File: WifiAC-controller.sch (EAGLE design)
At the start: 16 parts, among them U1 ATMEGA328P_TQFP

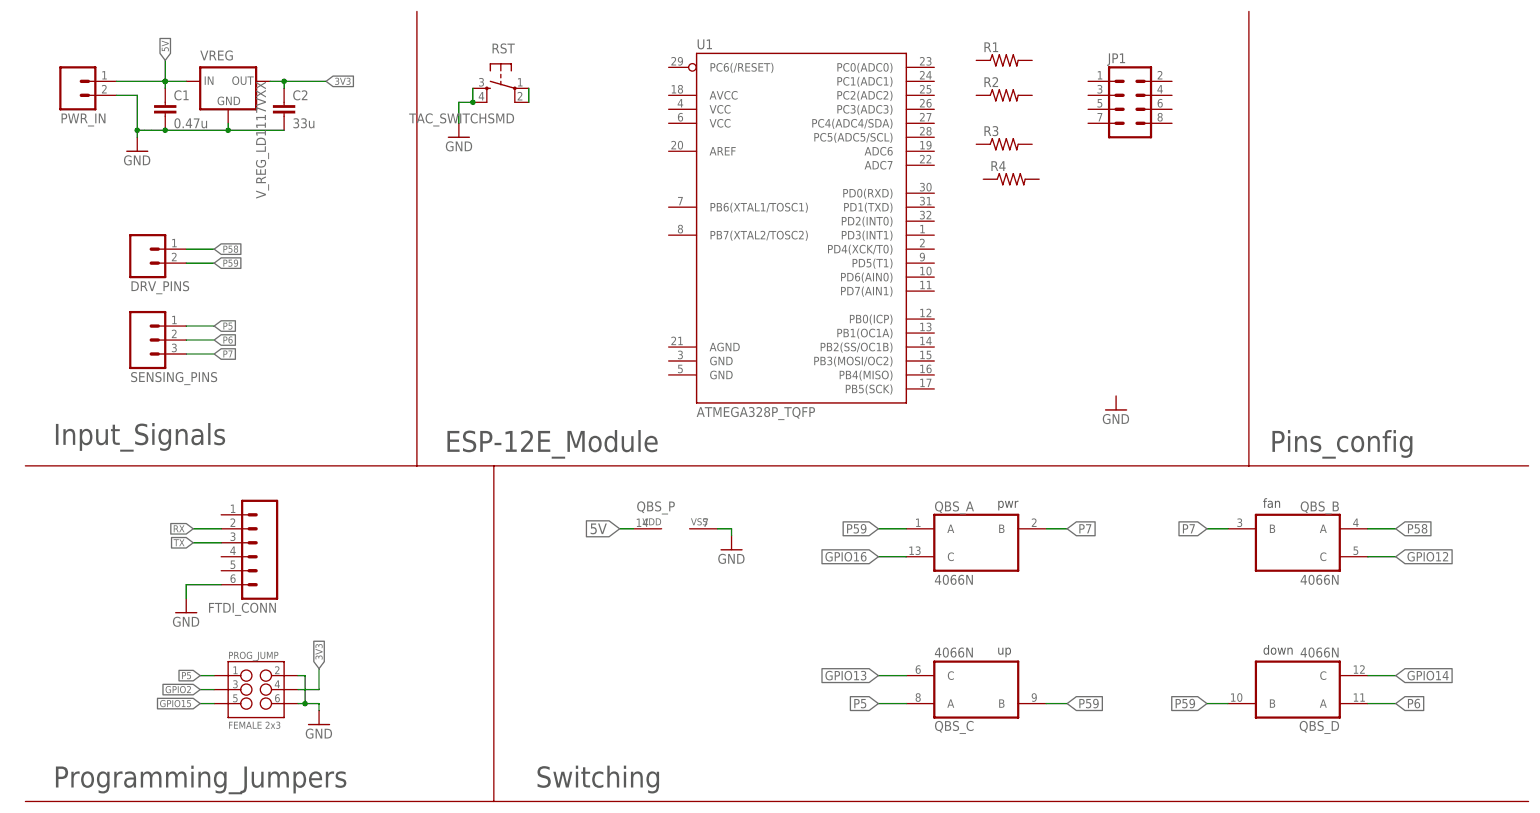
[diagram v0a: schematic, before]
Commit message: updated the circuit and the output file. circuit update includes changing the esp package and adding an atmega328 as mcu
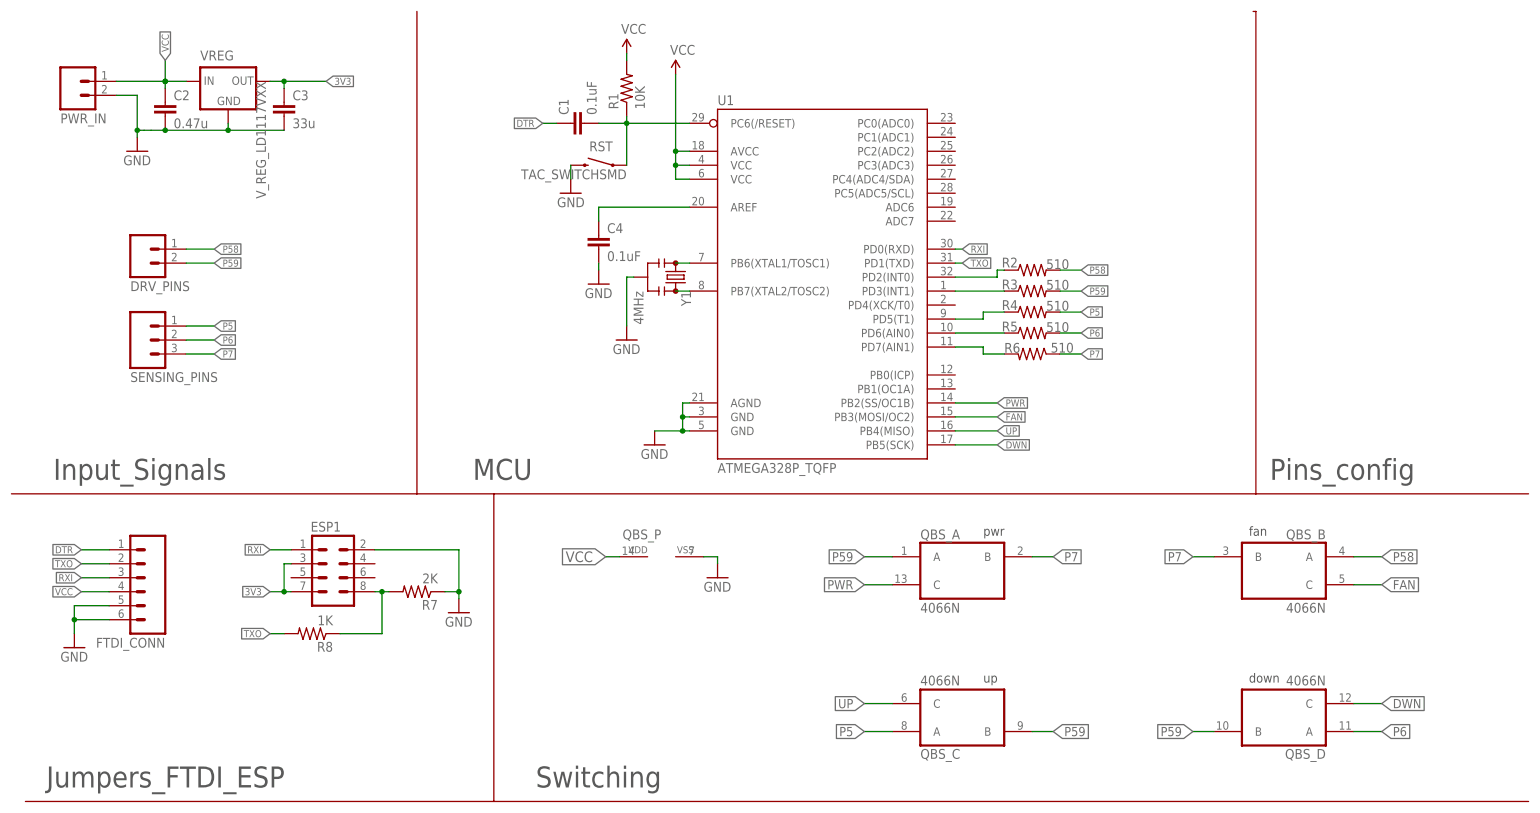
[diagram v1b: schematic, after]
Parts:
- removed JP1: (no value), SparkFun-Connectors:M04X2
- removed PROG_JUMP: FEMALE 2x3, SparkFun-Connectors:M03X2FEMALE
- added C3: 33u, SparkFun-Passives:CAPPTH2
- added C4: 0.1uF, SparkFun-Passives:CAP0805
- added ESP1: (no value), SparkFun-Connectors:M04X2
- added R5, R6: 510, SparkFun-Passives:RESISTOR0805-RES
- added R7: 2K, SparkFun-Passives:RESISTOR0805-RES
- added R8: 1K, SparkFun-Passives:RESISTOR0805-RES
- added Y1: 4MHz, SparkFun-FreqCtrl:RESONATOR4MHZ
- C1: value 0.47u -> 0.1uF; device SparkFun-Passives:CAPEZ -> SparkFun-Passives:CAP0805
- C2: value 33u -> 0.47u; device SparkFun-Passives:CAPPTH2 -> SparkFun-Passives:CAPEZ
- R1: value (none) -> 10K
- R2, R3, R4: value (none) -> 510
- RST: device SparkFun-Retired:TAC_SWITCHSMD -> SparkFun-Electromechanical:SWITCH-MOMENTARY-2SMD-REDUNDANT
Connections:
- removed net 5V: C1.1, PWR_IN.1, QBS_P.VDD, VREG.IN
- removed net GPIO12: QBS_B.C
- removed net GPIO13: QBS_C.C
- removed net GPIO14: QBS_D.C
- removed net GPIO15: PROG_JUMP.5
- removed net GPIO16: QBS_A.C
- removed net GPIO2: PROG_JUMP.3
- removed net RX: FTDI_CONN.2
- removed net TX: FTDI_CONN.3
- new net DTR: C1.1, FTDI_CONN.1
- new net DWN: QBS_D.C, U1.PB5(SCK)
- new net FAN: QBS_B.C, U1.PB3(MOSI/OC2)
- new net N$10: R6.2, U1.PD7(AIN1)
- new net N$14: ESP1.8, R7.2, R8.1
- new net N$3: C4.1, U1.AREF
- new net N$4: U1.PB6(XTAL1/TOSC1), Y1.1
- new net N$5: U1.PB7(XTAL2/TOSC2), Y1.3
- new net N$6: R2.1, U1.PD2(INT0)
- new net N$7: R3.1, U1.PD3(INT1)
- new net N$8: R4.1, U1.PD5(T1)
- new net N$9: R5.1, U1.PD6(AIN0)
- new net PWR: QBS_A.C, U1.PB2(SS/OC1B)
- new net RXI: ESP1.1, FTDI_CONN.3, U1.PD0(RXD)
- new net TXO: FTDI_CONN.2, R8.2, U1.PD1(TXD)
- new net UP: QBS_C.C, U1.PB4(MISO)
- new net VCC: C2.1, FTDI_CONN.4, PWR_IN.1, QBS_P.VDD, R1.2, U1.AVCC, U1.VCC@4, U1.VCC@6, VREG.IN
- net 3V3: now also C3.1, ESP1.3, ESP1.7; no longer C2.1, PROG_JUMP.4
- net GND: now also C3.2, C4.2, ESP1.2, FTDI_CONN.5, R7.1, RST.2, U1.AGND, U1.GND@3, U1.GND@5, Y1.2; no longer C1.2, PROG_JUMP.2, PROG_JUMP.6, RST.3, RST.4
- net N$1: now also C1.2, R1.1, U1.PC6(/RESET); no longer RST.2
- net P5: now also R4.2; no longer PROG_JUMP.1
- net P58: now also R2.2
- net P59: now also R3.2
- net P6: now also R5.2
- net P7: now also R6.1
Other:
- note added: "INPUT PINS P58->32(D2) P59->1(D3) P05->9(D5) P06->10(D6) P07->11(D7) OUTPUT PINS PWR->14(D10) FAN->15(D11) UP->16(D12) DWN->17(D13)"
- note added: "Jumpers_FTDI_ESP"
- note added: "MCU"
- note added: "This is a circuit that is implemented to make the AC controller in my room controlled using the wifi. The controller used is the arduino controller and an ESP 8266 the generic type."
- note removed: "ESP-12E_Module"
- note removed: "INPUT PINS"
- note removed: "OUTPUT PINS"
- note removed: "Programming_Jumpers"
- note removed: "The ESP packge is imported from the lib ESP-12.lbr"
- note removed: "The PROG_JUMP is a jumper used to change the mode of the chip in case a reprogramming is needed."
- note removed: "This is a circuit that is implemented to make the AC controller in my room controlled using the wifi."
- note removed: "down -> GPIO14"
- note removed: "fan -> GPIO12"
- note removed: "p5 -> GPIO0"
- note removed: "p58 -> GPIO9"
- note removed: "p59 -> GPIO10"
- note removed: "p6 -> GPIO5"
- note removed: "p7 -> GPIO4"
- note removed: "pwr -> GPIO16"
- note removed: "up -> GPIO13"
- moved on the sheet: C1, C2, FTDI_CONN, QBS_A, QBS_B, QBS_C, QBS_D, QBS_P, R1, R2, R3, R4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

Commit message: reouted the pcb
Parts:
- C2: device SparkFun-Passives:CAPEZ -> SparkFun-Passives:CAP0805
- C3: device SparkFun-Passives:CAPPTH2 -> SparkFun-Passives:CAP0805
- DRV_PINS, PWR_IN: device SparkFun-Connectors:M02LOCK_LONGPADS -> SparkFun-Connectors:M02POLAR
- SENSING_PINS: device SparkFun-Connectors:M03PTH -> SparkFun-Connectors:M03POLAR
- renumbered ESP1 to ESP8266
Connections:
- net P58: now also DRV_PINS.2; no longer DRV_PINS.1
- net P59: now also DRV_PINS.1; no longer DRV_PINS.2
